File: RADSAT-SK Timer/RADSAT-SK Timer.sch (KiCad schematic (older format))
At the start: 73 parts, among them J101 Conn_02x26_Odd_Even, J103 Conn_02x26_Odd_Even, Q101 IRLML2060, Q102 IRLML2060, Q103 IRLML2060, Q104 IRLML2060, Q105 IRLML2060, Q106 IRLML2060, Q107 IRLML2060, Q108 IRLML2060, Q109 IRLML2060, U101 LM397MF, U102 LM397MF, U103 LM397MF, U104 CD4052B

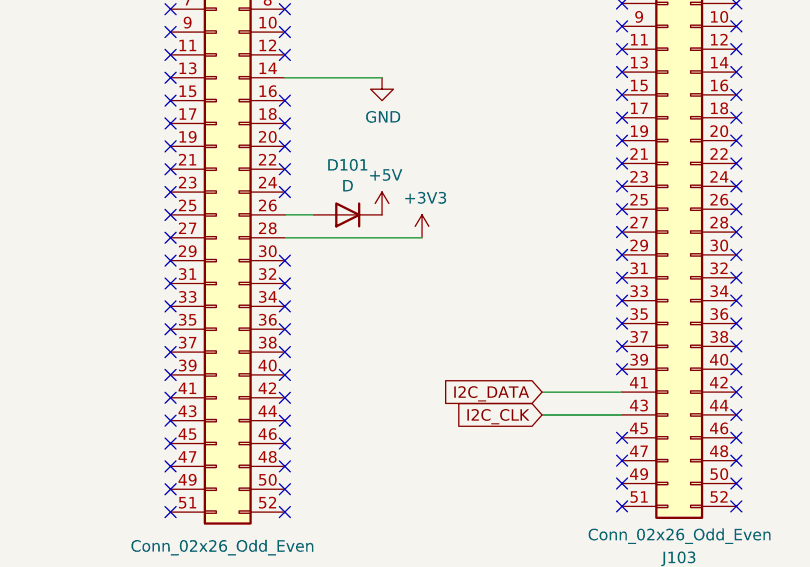
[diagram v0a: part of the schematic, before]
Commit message: Schematic: Added- 2 more inhibit ports Added- RBF Ports In and Out Connected USb Charger to connector H1-32. Layout: Port positioning and adjustments to some existing circuitry for better tracing.
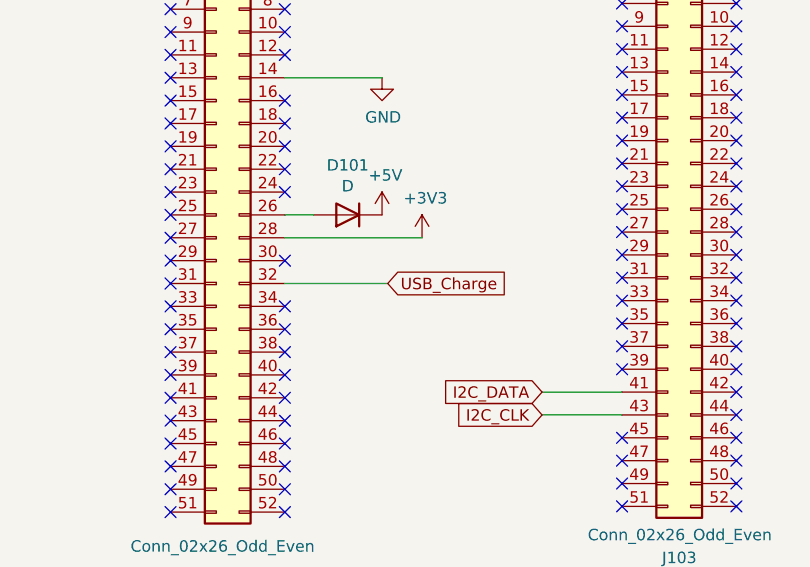
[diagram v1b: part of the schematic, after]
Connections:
- net labels added: USB_Charge
- wire segments 229 -> 230
- no-connect marks 99 -> 98
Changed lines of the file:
@@
 $EndComp
-Wire Wire Line
-	4200 2225 6225 2225
 Wire Wire Line
 	6225 750  6225 950
@@
 NoConn ~ 7875 4350
 NoConn ~ 8375 4350
-NoConn ~ 8375 4450
 NoConn ~ 7875 4450
 NoConn ~ 7875 4550
@@
 Wire Wire Line
 	2100 4900 2875 4900
+Wire Wire Line
+	4200 2225 6225 2225
+Wire Wire Line
+	8375 4450 8825 4450
+Text GLabel 8825 4450 2    50   Input ~ 0
+USB_Charge
 $EndSCHEMATC

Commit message: added starting place for RBF timer
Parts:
- Q101, Q102, Q103, Q104, Q105, Q106, Q107, Q108, Q109: symbol RADSAT-SK-Timer-rescue:IRLML2060-Transistor_FET -> Transistor_FET:IRLML2060
- U101, U102, U103: symbol RADSAT-SK-Timer-rescue:LM397MF-LM397MF -> LM397MF:LM397MF
- U104: symbol RADSAT-SK-Timer-rescue:CD4052B-Analog_Switch -> Analog_Switch:CD4052B
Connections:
- net labels removed: USB_Charge
- wire segments 230 -> 229
- no-connect marks 98 -> 99
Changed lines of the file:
@@
 EESchema Schematic File Version 4
-LIBS:RADSAT-SK Timer-cache
-EELAYER 26 0
+EELAYER 30 0
 EELAYER END
 $Descr A4 11693 8268
@@
 $EndComp
 $Comp
-L RADSAT-SK-Timer-rescue:CD4052B-Analog_Switch U104
+L Analog_Switch:CD4052B U104
 U 1 1 5FF9C3C1
 P 9125 1475
@@
 Wire Wire Line
 	8050 1675 8050 2175
-$Comp
-L power:+BATT #PWR0104
-U 1 1 601B4594
-P 2100 700
-F 0 "#PWR0104" H 2100 550 50  0001 C CNN
-F 1 "+BATT" H 2100 875 50  0000 C CNN
-F 2 "" H 2100 700 50  0001 C CNN
-F 3 "" H 2100 700 50  0001 C CNN
-	1    2100 700
-	1    0    0    -1
-$EndComp
 Wire Wire Line
 	9975 775  10625 775
@@
 Text Notes 7150 2675 0    79   ~ 0
 CSKB Connectors
-Wire Wire Line
-	2100 750  2100 700
-Connection ~ 2100 750
-Wire Wire Line
-	2100 750  1300 750
 Text Notes 525  6925 0    79   ~ 0
 Batteries, Charger, Booster, Mechanical Inhibits, Antenna Connector, Output Connectors
 $Comp
-L RADSAT-SK-Timer-rescue:IRLML2060-Transistor_FET Q104
+L Transistor_FET:IRLML2060 Q104
 U 1 1 600624B3
 P 1800 1525
@@
 $EndComp
 $Comp
-L RADSAT-SK-Timer-rescue:IRLML2060-Transistor_FET Q107
+L Transistor_FET:IRLML2060 Q107
 U 1 1 600655A8
 P 4300 1875
@@
 $EndComp
 $Comp
-L RADSAT-SK-Timer-rescue:IRLML2060-Transistor_FET Q101
+L Transistor_FET:IRLML2060 Q101
 U 1 1 6005D75A
 P 1200 1725
@@
 	600  750  600  1725
 $Comp
-L RADSAT-SK-Timer-rescue:LM397MF-LM397MF U101
+L LM397MF:LM397MF U101
 U 1 1 600CAF9B
 P 5525 1250
@@
 	1    0    0    -1
 $EndComp
+Wire Wire Line
+	4200 2225 6225 2225
 Wire Wire Line
 	6225 750  6225 950
@@
 	2100 2850 1300 2850
 $Comp
-L RADSAT-SK-Timer-rescue:IRLML2060-Transistor_FET Q105
+L Transistor_FET:IRLML2060 Q105
 U 1 1 6023BB16
 P 1800 3625
@@
 $EndComp
 $Comp
-L RADSAT-SK-Timer-rescue:IRLML2060-Transistor_FET Q108
+L Transistor_FET:IRLML2060 Q108
 U 1 1 6023BB1C
 P 4300 3975
@@
 $EndComp
 $Comp
-L RADSAT-SK-Timer-rescue:IRLML2060-Transistor_FET Q102
+L Transistor_FET:IRLML2060 Q102
 U 1 1 6023BB2E
 P 1200 3825
@@
 	600  2850 600  3825
 $Comp
-L RADSAT-SK-Timer-rescue:LM397MF-LM397MF U102
+L LM397MF:LM397MF U102
 U 1 1 6023BB41
 P 5525 3350
@@
 	2100 4900 1300 4900
 $Comp
-L RADSAT-SK-Timer-rescue:IRLML2060-Transistor_FET Q106
+L Transistor_FET:IRLML2060 Q106
 U 1 1 60268B09
 P 1800 5675
@@
 $EndComp
 $Comp
-L RADSAT-SK-Timer-rescue:IRLML2060-Transistor_FET Q109
+L Transistor_FET:IRLML2060 Q109
 U 1 1 60268B0F
 P 4300 6025
@@
 $EndComp
 $Comp
-L RADSAT-SK-Timer-rescue:IRLML2060-Transistor_FET Q103
+L Transistor_FET:IRLML2060 Q103
 U 1 1 60268B21
 P 1200 5875
@@
 	600  4900 600  5875
 $Comp
-L RADSAT-SK-Timer-rescue:LM397MF-LM397MF U103
+L LM397MF:LM397MF U103
 U 1 1 60268B34
 P 5525 5400
@@
 NoConn ~ 7875 4350
 NoConn ~ 8375 4350
+NoConn ~ 8375 4450
 NoConn ~ 7875 4450
 NoConn ~ 7875 4550
@@
 Connection ~ 8050 2175
 Wire Wire Line
+	2100 2850 2875 2850
+Wire Wire Line
+	2100 4900 2875 4900
+Wire Wire Line
 	2100 750  2875 750
 Wire Wire Line
-	2100 2850 2875 2850
-Wire Wire Line
-	2100 4900 2875 4900
-Wire Wire Line
-	4200 2225 6225 2225
-Wire Wire Line
-	8375 4450 8825 4450
-Text GLabel 8825 4450 2    50   Input ~ 0
-USB_Charge
+	2100 750  1300 750
+Connection ~ 2100 750
+Wire Wire Line
+	2100 750  2100 700
+$Comp
+L power:+BATT #PWR0104
+U 1 1 601B4594
+P 2100 700
+F 0 "#PWR0104" H 2100 550 50  0001 C CNN
+F 1 "+BATT" H 2100 875 50  0000 C CNN
+F 2 "" H 2100 700 50  0001 C CNN
+F 3 "" H 2100 700 50  0001 C CNN
+	1    2100 700
+	1    0    0    -1
+$EndComp
 $EndSCHEMATC

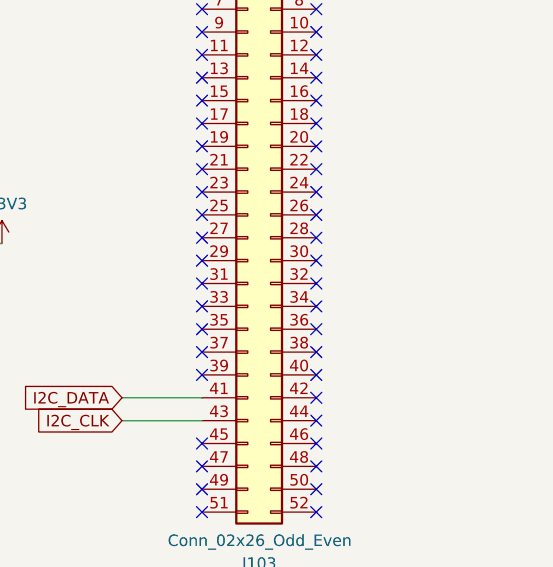
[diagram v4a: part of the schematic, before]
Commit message: 1.Added USB Header, Footprint and lib files 2. got rid of the rescue library by reassigning the symbols to proper libraries in the project 3. assigned footprints to all components, though BOM still MIA. Diode MBRM appears to be discontinues on digikey???
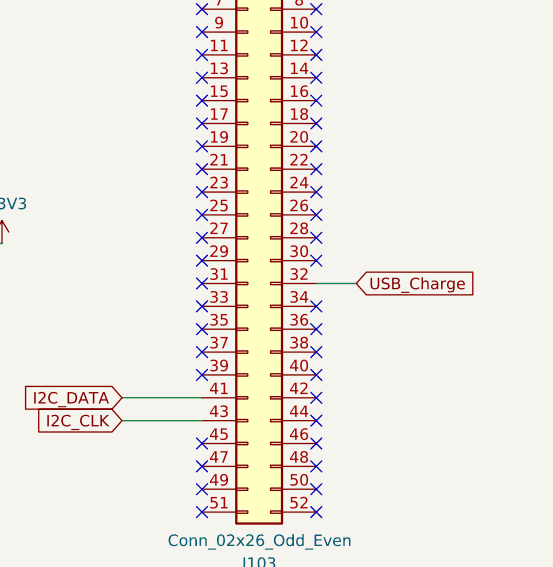
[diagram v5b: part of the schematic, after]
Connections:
- net USB_Charge: now reaches J103.32 (Pin_32)
- no-connect marks 99 -> 98
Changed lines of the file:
@@
 NoConn ~ 9850 4325
 NoConn ~ 9850 4425
-NoConn ~ 10350 4425
 NoConn ~ 10350 4525
 NoConn ~ 9850 4525
@@
 	1    0    0    -1
 $EndComp
+Text GLabel 10525 4425 2    50   Input ~ 0
+USB_Charge
+Wire Wire Line
+	10525 4425 10350 4425
 $EndSCHEMATC

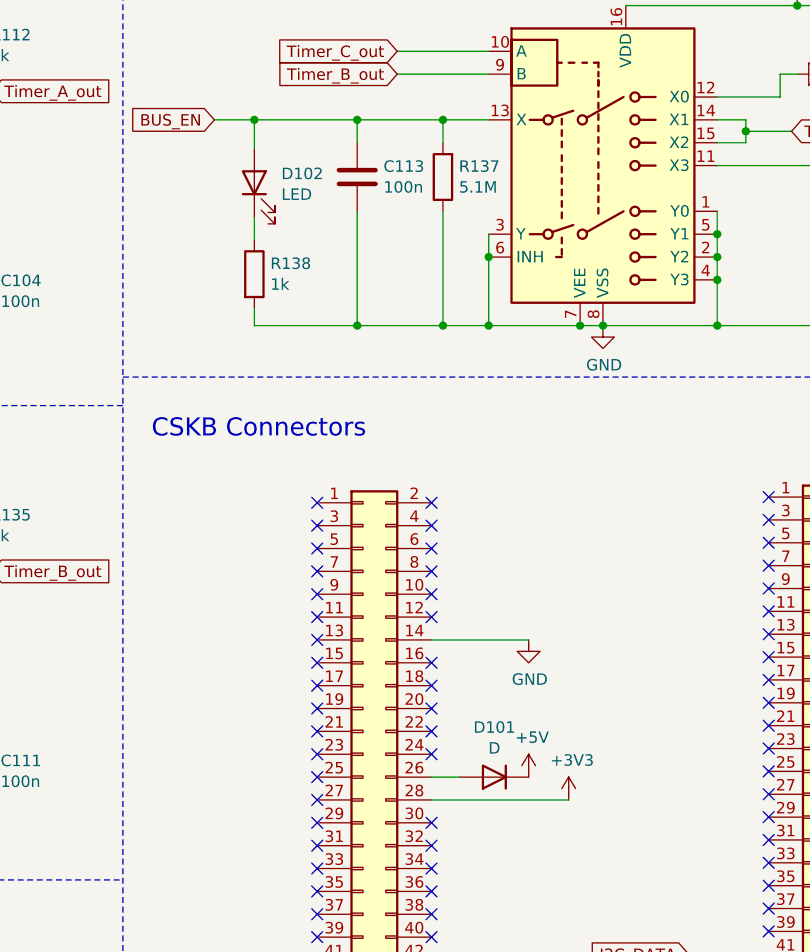
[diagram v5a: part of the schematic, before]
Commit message: added pchannel JFET and Diode logic for inhibitors, edited the layout a bit still not final
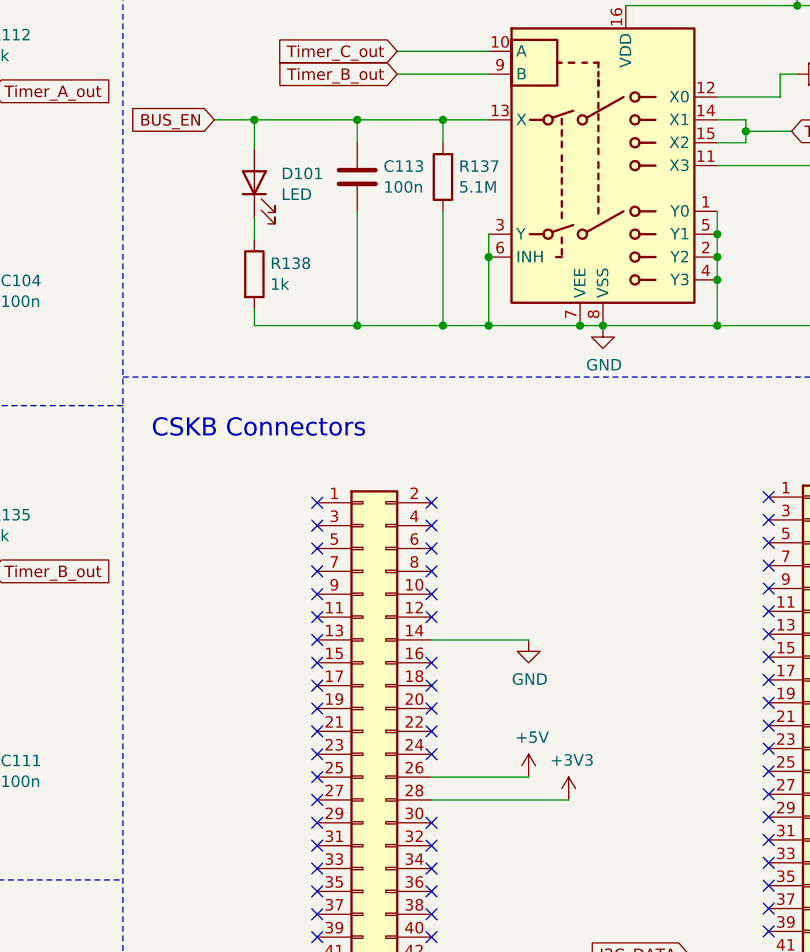
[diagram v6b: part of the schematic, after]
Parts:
- removed D101: D, Diode_SMD:D_0805_2012Metric, symbol Device:D
- renumbered D102 to D101
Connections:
- net +5V: now also J101.26 (Pin_26)
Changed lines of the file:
@@
-	1    0    0    -1
-$EndComp
-$Comp
-L power:+5V #PWR0114
-U 1 1 6039ECF2
-P 8800 4150
-F 0 "#PWR0114" H 8800 4000 50  0001 C CNN
-F 1 "+5V" H 8815 4323 50  0000 C CNN
-F 2 "" H 8800 4150 50  0001 C CNN
-F 3 "" H 8800 4150 50  0001 C CNN
-	1    8800 4150
-	1    0    0    -1
-$EndComp
-$Comp
-L power:+3V3 #PWR0115
-U 1 1 603B0D07
-P 8975 4250
-F 0 "#PWR0115" H 8975 4100 50  0001 C CNN
-F 1 "+3V3" H 8990 4423 50  0000 C CNN
-F 2 "" H 8975 4250 50  0001 C CNN
-F 3 "" H 8975 4250 50  0001 C CNN
-	1    8975 4250
 	1    0    0    -1
 $EndComp
@@
 NoConn ~ 9850 5425
 NoConn ~ 10350 5425
-$Comp
-L Device:D D101
-U 1 1 600DAD15
-P 8650 4150
-F 0 "D101" H 8650 3933 50  0000 C CNN
-F 1 "D" H 8650 4024 50  0000 C CNN
-F 2 "Diode_SMD:D_0805_2012Metric" H 8650 4150 50  0001 C CNN
-F 3 "~" H 8650 4150 50  0001 C CNN
-	1    8650 4150
-	-1   0    0    1
-$EndComp
 Wire Wire Line
 	9500 4925 9850 4925
@@
 $EndComp
 Wire Wire Line
-	8500 4150 8375 4150
-Wire Wire Line
-	8375 4250 8975 4250
-Wire Wire Line
 	8375 3550 8800 3550
 NoConn ~ 10350 3525
@@
 NoConn ~ 10350 4125
 $Comp
-L Device:LED D102
+L Device:LED D101
 U 1 1 600FEA55
 P 7600 1550
-F 0 "D102" V 7639 1432 50  0000 R CNN
+F 0 "D101" V 7639 1432 50  0000 R CNN
 F 1 "LED" V 7548 1432 50  0000 R CNN
 F 2 "LED_SMD:LED_0805_2012Metric" H 7600 1550 50  0001 C CNN
@@
 Wire Wire Line
 	10525 4425 10350 4425
+$Comp
+L power:+5V #PWR0114
+U 1 1 6039ECF2
+P 8800 4150
+F 0 "#PWR0114" H 8800 4000 50  0001 C CNN
+F 1 "+5V" H 8815 4323 50  0000 C CNN
+F 2 "" H 8800 4150 50  0001 C CNN
+F 3 "" H 8800 4150 50  0001 C CNN
+	1    8800 4150
+	1    0    0    -1
+$EndComp
+Wire Wire Line
+	8375 4250 8975 4250
+$Comp
+L power:+3V3 #PWR0115
+U 1 1 603B0D07
+P 8975 4250
+F 0 "#PWR0115" H 8975 4100 50  0001 C CNN
+F 1 "+3V3" H 8990 4423 50  0000 C CNN
+F 2 "" H 8975 4250 50  0001 C CNN
+F 3 "" H 8975 4250 50  0001 C CNN
+	1    8975 4250
+	1    0    0    -1
+$EndComp
+Wire Wire Line
+	8375 4150 8800 4150
 $EndSCHEMATC

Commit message: This commit contains more ccomponent sourcing, mainly a diode array for the inhibitor logic diodes, handsoldering footprints have been chosen for some of the sourced components, see BOM, this should help us save time and frustration in handsoldering the testboard, SW connectors were reorganized to make better connections and now both side panels must be closed to connect the battery
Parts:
- D101: footprint LED_SMD:LED_0805_2012Metric -> LED_SMD:LED_0603_1608Metric_Pad1.05x0.95mm_HandSolder
- Q101, Q102, Q103, Q104, Q105, Q106, Q107, Q108, Q109: footprint Package_TO_SOT_SMD:SOT-23 -> Package_TO_SOT_SMD:SOT-23_Handsoldering
- U101, U102, U103: footprint Package_TO_SOT_SMD:TSOT-23-5 -> Package_TO_SOT_SMD:TSOT-23-5_HandSoldering
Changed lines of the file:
@@
 F 0 "Q104" H 2004 1571 50  0000 L CNN
 F 1 "IRLML2060" H 2004 1480 50  0000 L CNN
-F 2 "Package_TO_SOT_SMD:SOT-23" H 2000 1450 50  0001 L CIN
+F 2 "Package_TO_SOT_SMD:SOT-23_Handsoldering" H 2000 1450 50  0001 L CIN
 F 3 "https://www.infineon.com/dgdl/irlml2060pbf.pdf?fileId=5546d462533600a401535664b7fb25ee" H 1800 1525 50  0001 L CNN
 	1    1800 1525
@@
 F 0 "Q107" H 4075 1800 50  0000 L CNN
 F 1 "IRLML2060" H 3975 1700 50  0000 L CNN
-F 2 "Package_TO_SOT_SMD:SOT-23" H 4500 1800 50  0001 L CIN
+F 2 "Package_TO_SOT_SMD:SOT-23_Handsoldering" H 4500 1800 50  0001 L CIN
 F 3 "https://www.infineon.com/dgdl/irlml2060pbf.pdf?fileId=5546d462533600a401535664b7fb25ee" H 4300 1875 50  0001 L CNN
 	1    4300 1875
@@
 F 0 "Q101" H 1404 1771 50  0000 L CNN
 F 1 "IRLML2060" H 1404 1680 50  0000 L CNN
-F 2 "Package_TO_SOT_SMD:SOT-23" H 1400 1650 50  0001 L CIN
+F 2 "Package_TO_SOT_SMD:SOT-23_Handsoldering" H 1400 1650 50  0001 L CIN
 F 3 "https://www.infineon.com/dgdl/irlml2060pbf.pdf?fileId=5546d462533600a401535664b7fb25ee" H 1200 1725 50  0001 L CNN
 	1    1200 1725
@@
 F 0 "U101" H 5525 1450 50  0000 C CNN
 F 1 "LM397MF" H 5525 1275 50  0000 C CNN
-F 2 "Package_TO_SOT_SMD:TSOT-23-5" H 5525 1250 50  0001 L BNN
+F 2 "Package_TO_SOT_SMD:TSOT-23-5_HandSoldering" H 5525 1250 50  0001 L BNN
 F 3 "" H 5525 1250 50  0001 L BNN
 	1    5525 1250
@@
 F 0 "Q105" H 2004 3671 50  0000 L CNN
 F 1 "IRLML2060" H 2004 3580 50  0000 L CNN
-F 2 "Package_TO_SOT_SMD:SOT-23" H 2000 3550 50  0001 L CIN
+F 2 "Package_TO_SOT_SMD:SOT-23_Handsoldering" H 2000 3550 50  0001 L CIN
 F 3 "https://www.infineon.com/dgdl/irlml2060pbf.pdf?fileId=5546d462533600a401535664b7fb25ee" H 1800 3625 50  0001 L CNN
 	1    1800 3625
@@
 F 0 "Q108" H 4075 3900 50  0000 L CNN
 F 1 "IRLML2060" H 3975 3800 50  0000 L CNN
-F 2 "Package_TO_SOT_SMD:SOT-23" H 4500 3900 50  0001 L CIN
+F 2 "Package_TO_SOT_SMD:SOT-23_Handsoldering" H 4500 3900 50  0001 L CIN
 F 3 "https://www.infineon.com/dgdl/irlml2060pbf.pdf?fileId=5546d462533600a401535664b7fb25ee" H 4300 3975 50  0001 L CNN
 	1    4300 3975
@@
 F 0 "Q102" H 1404 3871 50  0000 L CNN
 F 1 "IRLML2060" H 1404 3780 50  0000 L CNN
-F 2 "Package_TO_SOT_SMD:SOT-23" H 1400 3750 50  0001 L CIN
+F 2 "Package_TO_SOT_SMD:SOT-23_Handsoldering" H 1400 3750 50  0001 L CIN
 F 3 "https://www.infineon.com/dgdl/irlml2060pbf.pdf?fileId=5546d462533600a401535664b7fb25ee" H 1200 3825 50  0001 L CNN
 	1    1200 3825
@@
 F 0 "U102" H 5525 3550 50  0000 C CNN
 F 1 "LM397MF" H 5525 3375 50  0000 C CNN
-F 2 "Package_TO_SOT_SMD:TSOT-23-5" H 5525 3350 50  0001 L BNN
+F 2 "Package_TO_SOT_SMD:TSOT-23-5_HandSoldering" H 5525 3350 50  0001 L BNN
 F 3 "" H 5525 3350 50  0001 L BNN
 	1    5525 3350
@@
 F 0 "Q106" H 2004 5721 50  0000 L CNN
 F 1 "IRLML2060" H 2004 5630 50  0000 L CNN
-F 2 "Package_TO_SOT_SMD:SOT-23" H 2000 5600 50  0001 L CIN
+F 2 "Package_TO_SOT_SMD:SOT-23_Handsoldering" H 2000 5600 50  0001 L CIN
 F 3 "https://www.infineon.com/dgdl/irlml2060pbf.pdf?fileId=5546d462533600a401535664b7fb25ee" H 1800 5675 50  0001 L CNN
 	1    1800 5675
@@
 F 0 "Q109" H 4075 5950 50  0000 L CNN
 F 1 "IRLML2060" H 3975 5850 50  0000 L CNN
-F 2 "Package_TO_SOT_SMD:SOT-23" H 4500 5950 50  0001 L CIN
+F 2 "Package_TO_SOT_SMD:SOT-23_Handsoldering" H 4500 5950 50  0001 L CIN
 F 3 "https://www.infineon.com/dgdl/irlml2060pbf.pdf?fileId=5546d462533600a401535664b7fb25ee" H 4300 6025 50  0001 L CNN
 	1    4300 6025
@@
 F 0 "Q103" H 1404 5921 50  0000 L CNN
 F 1 "IRLML2060" H 1404 5830 50  0000 L CNN
-F 2 "Package_TO_SOT_SMD:SOT-23" H 1400 5800 50  0001 L CIN
+F 2 "Package_TO_SOT_SMD:SOT-23_Handsoldering" H 1400 5800 50  0001 L CIN
 F 3 "https://www.infineon.com/dgdl/irlml2060pbf.pdf?fileId=5546d462533600a401535664b7fb25ee" H 1200 5875 50  0001 L CNN
 	1    1200 5875
@@
 F 0 "U103" H 5525 5600 50  0000 C CNN
 F 1 "LM397MF" H 5525 5425 50  0000 C CNN
-F 2 "Package_TO_SOT_SMD:TSOT-23-5" H 5525 5400 50  0001 L BNN
+F 2 "Package_TO_SOT_SMD:TSOT-23-5_HandSoldering" H 5525 5400 50  0001 L BNN
 F 3 "" H 5525 5400 50  0001 L BNN
 	1    5525 5400
@@
 F 0 "D101" V 7639 1432 50  0000 R CNN
 F 1 "LED" V 7548 1432 50  0000 R CNN
-F 2 "LED_SMD:LED_0805_2012Metric" H 7600 1550 50  0001 C CNN
+F 2 "LED_SMD:LED_0603_1608Metric_Pad1.05x0.95mm_HandSolder" H 7600 1550 50  0001 C CNN
 F 3 "~" H 7600 1550 50  0001 C CNN
 	1    7600 1550

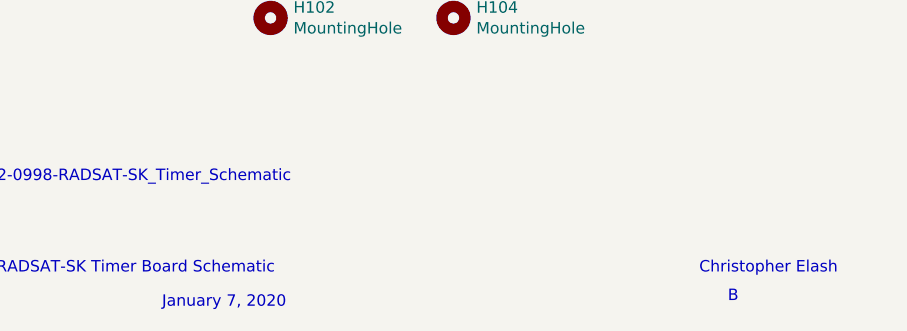
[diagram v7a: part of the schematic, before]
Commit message: Noticed that the source on all of the schematic 2 transistors were wrong and needed to be flipped, except on the rbf where it is intentional q Q ~
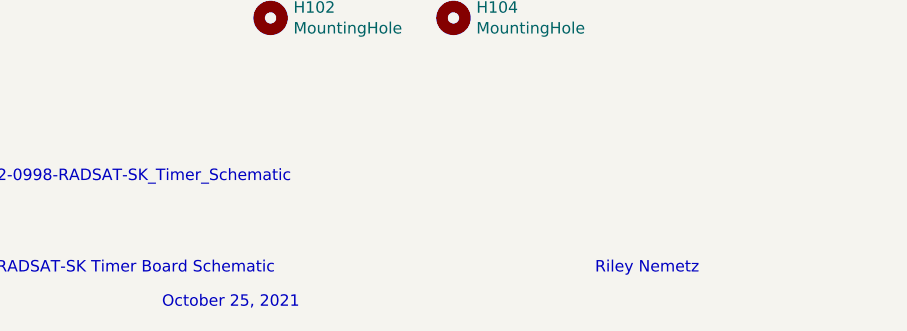
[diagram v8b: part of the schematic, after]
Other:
- note added: "October 25, 2021\n"
- note added: "Riley Nemetz"
- note removed: "B"
- note removed: "Christopher Elash"
- note removed: "January 7, 2020"
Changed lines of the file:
@@
 RADSAT-SK Timer Board Schematic
 Text Notes 8125 7650 0    50   ~ 0
-January 7, 2020
+October 25, 2021\n
 Text Notes 7000 7100 0    50   ~ 0
 CCP-ELEC-32-0998-RADSAT-SK_Timer_Schematic
-Text Notes 10475 7500 0    50   ~ 0
-Christopher Elash
-Text Notes 10600 7625 0    50   ~ 0
-B
+Text Notes 10475 7500 2    50   ~ 0
+Riley Nemetz
 $Comp
 L Device:R R103
